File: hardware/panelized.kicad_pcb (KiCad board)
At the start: 2 copper layers, 69.2 x 21 mm, 86 parts, among them J1 USB_B_Micro, J12 Conn_01x01, J2 Conn_01x01, J3 Conn_01x01, J4 Conn_01x01, Q1 Q_DUAL_NPN_NPN_E1B1C2E2B2C1, Q2 Q_PMOS_GSD, Q3 Q_PMOS_GSD, U1 MCP73831-2-OT, U2 CP2104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

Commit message: Updated panel gerber to v2.6
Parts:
- removed R5 (x2): 1GΩ, Resistor_SMD:R_0201_0603Metric
- added JP1: Jumper_NO_Small, Resistor_SMD:R_0201_0603Metric, F.Cu at (137.5, 112.8)
- added JP1: Jumper_NO_Small, Resistor_SMD:R_0201_0603Metric, F.Cu at (137.5, 100.8)
- R11 (x2): value 324kΩ -> 330kΩ
- R12 (x2): value 348kΩ -> 330kΩ
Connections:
- U2 pad : 0V -> (no net)
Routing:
- net 0V: track 192.1 -> 196.4 mm, vias 36 -> 50
- net (no net): track 720.1 -> 716.0 mm, vias 40 -> 42
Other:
- board text added: "Double-Oh v2.5 // August 2020"
- board text removed: "Double-Oh v2.4 // July 2020"

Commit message: Updated gerbers
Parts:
- added U5: BD48KxxG, Package_TO_SOT_SMD:SOT-23, B.Cu at (103.3, 114.0)
- added U5: BD48KxxG, Package_TO_SOT_SMD:SOT-23, B.Cu at (103.3, 102.0)
- R12 (x2): value 330kΩ -> 300kΩ
- R9 (x2): value 480kΩ -> 470kΩ
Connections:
- C1 pad 1: 0V -> (no net) (x2)
- C10 pad 1: 0V -> (no net) (x2)
- C11 pad 2: 0V -> (no net) (x2)
- C13 pad 1: 0V -> (no net) (x2)
- C2 pad 1: 0V -> (no net) (x2)
- C5 pad 2: 0V -> (no net) (x2)
- C7 pad 1: 0V -> (no net) (x2)
- D2 pad 2: 0V -> (no net) (x2)
- J1 pad 5: 0V -> (no net) (x2)
- J4 pad 1: 0V -> (no net) (x2)
- JP1 pad 1: 0V -> (no net) (x2)
- R10 pad 1: 0V -> (no net) (x2)
- R14 pad 1: 0V -> (no net) (x2)
- R2 pad 1: 0V -> (no net) (x2)
- R3 pad 2: 0V -> (no net) (x2)
- R6 pad 2: 0V -> (no net) (x2)
- U1 pad 2: 0V -> (no net) (x2)
- U2 pad 2: 0V -> (no net) (x2)
- U2 pad 25: 0V -> (no net) (x2)
- U3 pad 11: 0V -> (no net) (x2)
- U3 pad 2: 0V -> (no net) (x2)
- U3 pad 8: 0V -> (no net) (x2)
- U4 pad 49: 0V -> (no net) (x2)
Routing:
- net (no net): track 716.0 -> 932.3 mm, vias 42 -> 96
- net 0V: track 196.4 -> 0.00 mm, vias 50 -> 0
- added copper zone on B.Cu, net (none)
- removed copper zone on B.Cu, net 0V
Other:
- board text added: "Double-Oh v2.6 // August 2020"
- board text removed: "Double-Oh v2.5 // August 2020"

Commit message: Gerbers updated
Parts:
- removed the U5 at (103.3, 114.0)
- removed the U5 at (103.3, 102.0)
- added R5: 470kΩ, Resistor_SMD:R_0603_1608Metric_Pad1.05x0.95mm_HandSolder, B.Cu at (107.2, 102.3)
- added R5: 470kΩ, Resistor_SMD:R_0603_1608Metric_Pad1.05x0.95mm_HandSolder, B.Cu at (107.2, 114.3)
- added U5: BD48KxxG, Package_TO_SOT_SMD:SOT-23, B.Cu at (103.7, 101.7)
- added U5: BD48KxxG, Package_TO_SOT_SMD:SOT-23, B.Cu at (103.7, 113.7)
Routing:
- net (no net): track 932.3 -> 914.6 mm, vias 96 -> 94

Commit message: Update gerbers to 2.7
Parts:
- removed the C1 at (114.8, 105.0)
- removed the C1 at (114.8, 117.0)
- removed the C10 at (110.0, 103.0)
- removed the C10 at (110.0, 115.0)
- removed the R2 at (114.8, 106.3)
- removed the R2 at (114.8, 118.3)
- removed the R3 at (117.7, 106.3)
- removed the R3 at (117.7, 118.3)
- removed the R5 at (107.2, 102.3)
- removed the R5 at (107.2, 114.3)
- added C1: 4.7μF, Capacitor_SMD:C_0402_1005Metric, F.Cu at (114.8, 106.5)
- added C1: 4.7μF, Capacitor_SMD:C_0402_1005Metric, F.Cu at (114.8, 118.5)
- added C10: 10μF, Capacitor_SMD:C_0402_1005Metric, F.Cu at (110.0, 102.8)
- added C10: 10μF, Capacitor_SMD:C_0402_1005Metric, F.Cu at (110.0, 114.8)
- added R2: 3kΩ, Resistor_SMD:R_0402_1005Metric, F.Cu at (114.8, 105.0)
- added R2: 3kΩ, Resistor_SMD:R_0402_1005Metric, F.Cu at (114.8, 117.0)
- added R3: 68kΩ, Resistor_SMD:R_0402_1005Metric, F.Cu at (117.7, 105.9)
- added R3: 68kΩ, Resistor_SMD:R_0402_1005Metric, F.Cu at (117.7, 117.9)
- added R5: 470kΩ, Resistor_SMD:R_0402_1005Metric, F.Cu at (103.3, 101.4)
- added R5: 470kΩ, Resistor_SMD:R_0402_1005Metric, F.Cu at (103.3, 113.4)
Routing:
- net (no net): track 914.6 -> 915.2 mm, vias 94 -> 92
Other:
- board text added: "Double-Oh v2.7 // Sept. 2020"
- board text removed: "Double-Oh v2.6 // August 2020"

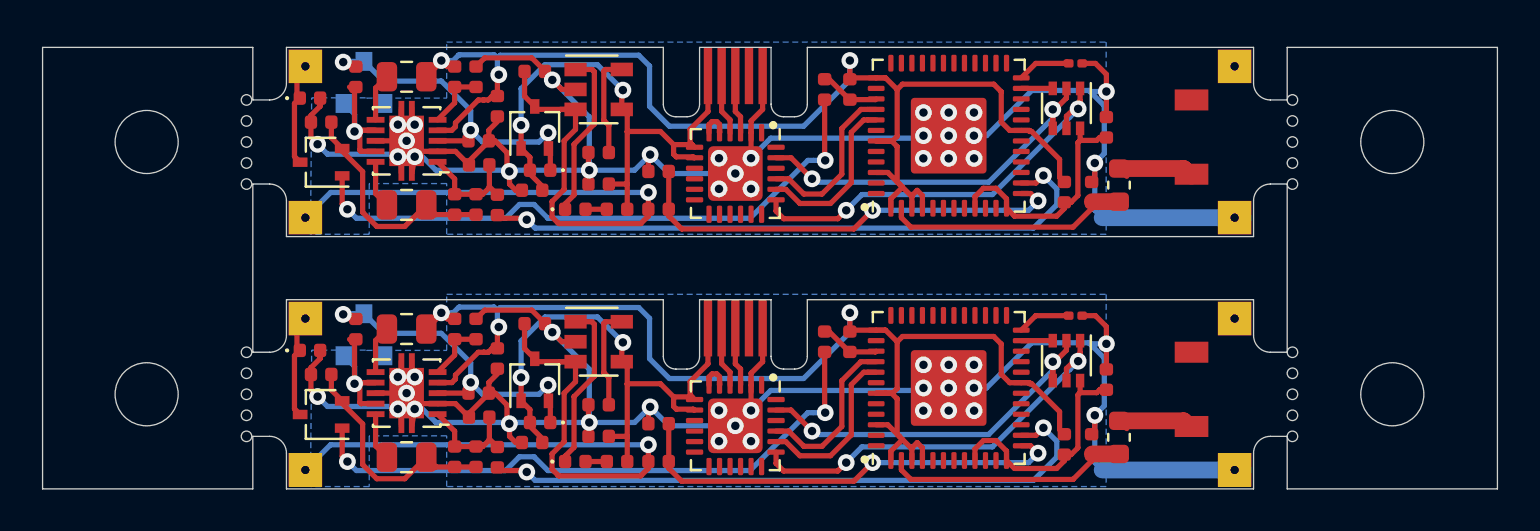
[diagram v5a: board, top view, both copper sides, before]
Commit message: Switched to a new, smaller voltage supervisor
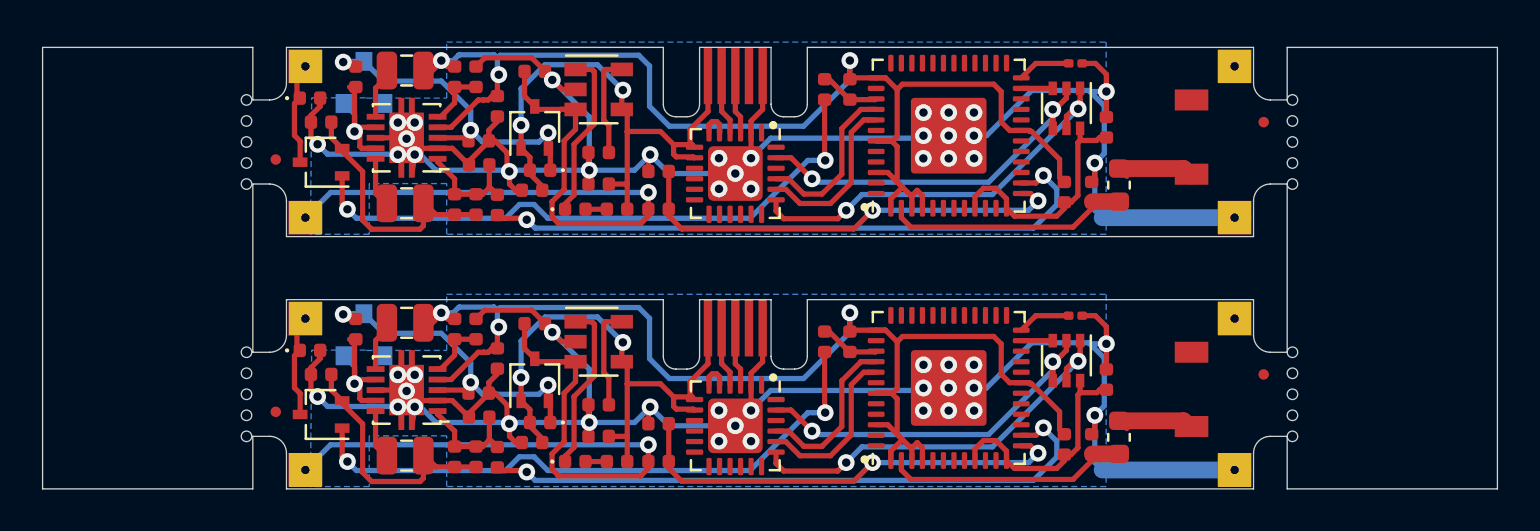
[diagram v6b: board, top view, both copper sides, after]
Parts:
- removed the L2 at (105.7, 101.4)
- removed the L2 at (105.7, 113.4)
- removed the L3 at (105.7, 107.5)
- removed the L3 at (105.7, 119.5)
- removed the U3 at (105.7, 104.4)
- removed the U3 at (105.7, 116.4)
- added G***: LOGO, double-oh:OSHW_mark, B.Cu at (112.8, 115.3)
- added G***: LOGO, double-oh:OSHW_mark, B.Cu at (112.8, 103.3)
- added L2: 2.2μH, double-oh:L_0806_2016Metric, F.Cu at (105.7, 113.1)
- added L2: 2.2μH, double-oh:L_0806_2016Metric, F.Cu at (105.7, 101.1)
- added L3: 2.2μH, double-oh:L_0806_2016Metric, F.Cu at (105.7, 119.4)
- added L3: 2.2μH, double-oh:L_0806_2016Metric, F.Cu at (105.7, 107.4)
- added REF**: Fiducial_0.5mm_Mask1.5mm, Fiducial:Fiducial_0.5mm_Mask1.5mm, F.Cu at (146.5, 115.6)
- added REF**: Fiducial_0.5mm_Mask1.5mm, Fiducial:Fiducial_0.5mm_Mask1.5mm, F.Cu at (99.5, 117.3)
- added REF**: Fiducial_0.5mm_Mask1.5mm, Fiducial:Fiducial_0.5mm_Mask1.5mm, F.Cu at (146.5, 103.6)
- added REF**: Fiducial_0.5mm_Mask1.5mm, Fiducial:Fiducial_0.5mm_Mask1.5mm, F.Cu at (99.5, 105.3)
- added U3: TPS62400, Package_SON:VSON-10-1EP_3x3mm_P0.5mm_EP1.65x2.4mm, F.Cu at (105.7, 116.3)
- added U3: TPS62400, Package_SON:VSON-10-1EP_3x3mm_P0.5mm_EP1.65x2.4mm, F.Cu at (105.7, 104.3)
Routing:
- net (no net): track 915.2 -> 916.8 mm
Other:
- rule pad_to_mask_clearance: 0.051 -> 0
